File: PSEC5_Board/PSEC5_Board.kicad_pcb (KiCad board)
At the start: 6 copper layers, 76.2 x 76.2 mm, 187 parts, among them IC1 LTC6409IUDB#TRMPBF, IC2 LTC6409IUDB#TRMPBF, IC3 LTC6409IUDB#TRMPBF, IC4 LTC6409IUDB#TRMPBF, IC5 LTC6409IUDB#TRMPBF, IC6 LTC6409IUDB#TRMPBF, IC7 LTC6409IUDB#TRMPBF, IC8 LTC6409IUDB#TRMPBF, J1 QTH-040-01-X-D-DP-A, J11 Conn_Coaxial, J2 Conn_Coaxial, J3 Conn_Coaxial, J4 Conn_Coaxial, J5 Conn_Coaxial, J6 Conn_Coaxial, J7 Conn_Coaxial, J8 Conn_Coaxial, J9 QTH-040-01-X-D-DP-A, U1 MCP1700T-1802E_TT, U3 DAC8411IDCKT, U4 MC100LVEL40DWG, U6 OPA607QDBVRQ1, U7 AD4008BCPZ-RL7, Y1 ASE2-40.000MHZ-ET

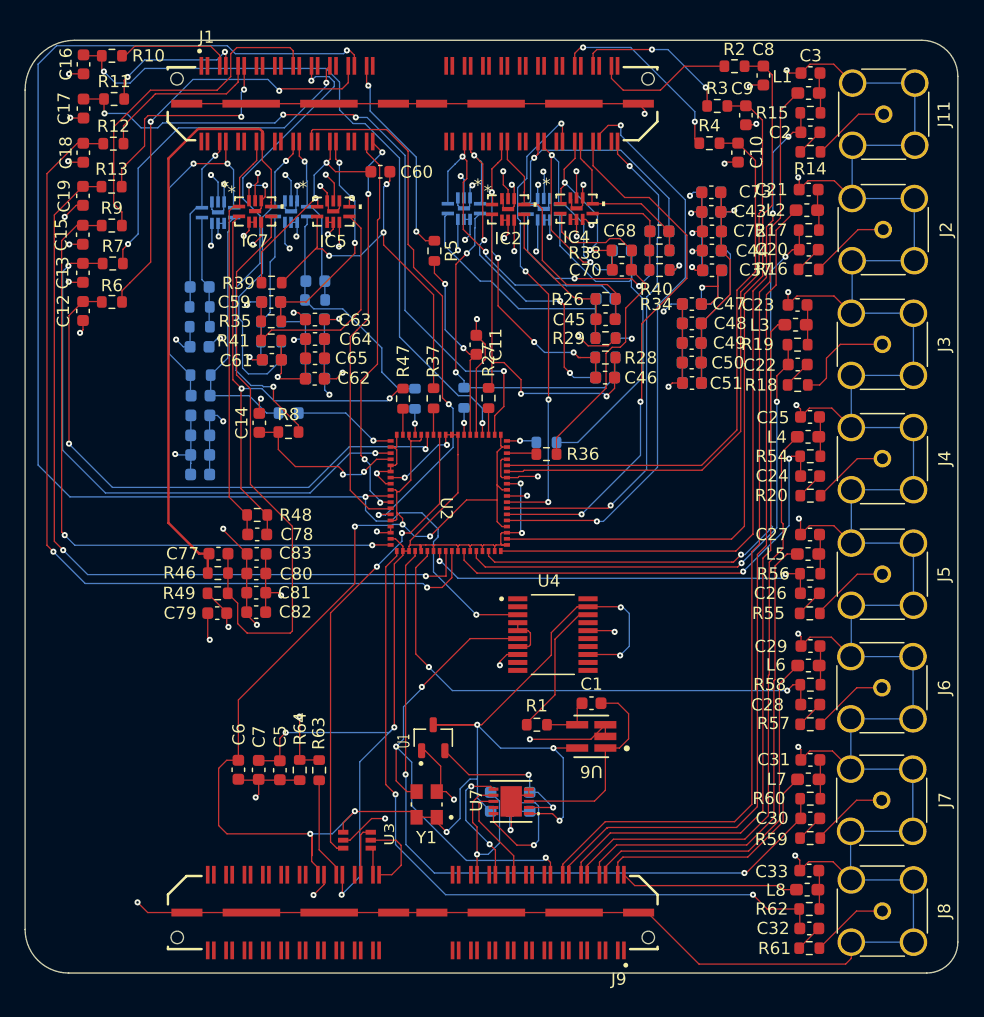
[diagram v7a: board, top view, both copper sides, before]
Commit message: DUT v4 Push
Addressed the issues discussed in last week's meeting, cleared ERC errors, still any warnings with Solder Mask.
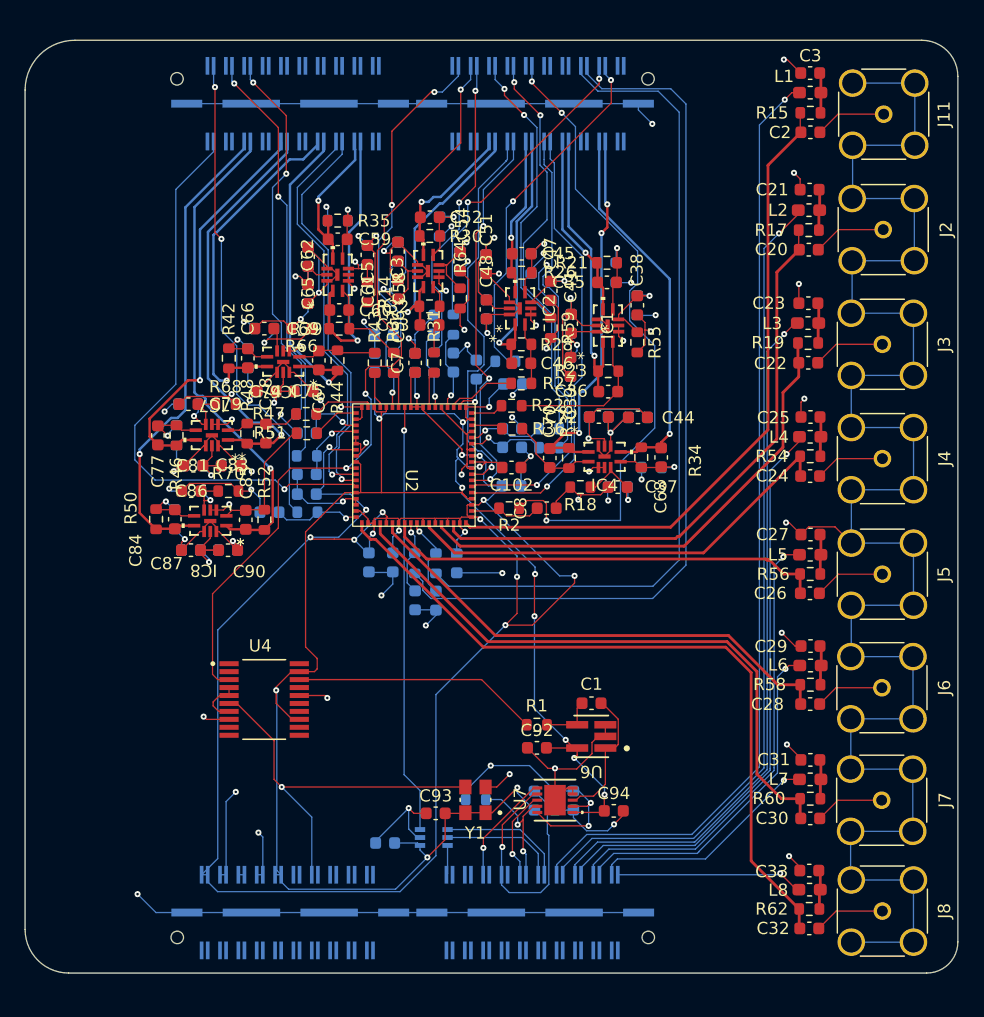
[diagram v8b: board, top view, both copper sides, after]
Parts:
- removed C6: 400n, Capacitor_SMD:C_0603_1608Metric
- removed U1: MCP1700T-1802E_TT, MCP1700T_1802E_TT:SOT95P237X112-3N
- added C100: 680n, Capacitor_SMD:C_0603_1608Metric, B.Cu at (145.0, 86.5)
- added C101: 100n, Capacitor_SMD:C_0603_1608Metric, B.Cu at (143.0, 86.5)
- added C102: 100n, Capacitor_SMD:C_0603_1608Metric, F.Cu at (154.7, 78.7)
- added C91: 0.1u, Capacitor_SMD:C_0603_1608Metric, B.Cu at (144.3, 109.4)
- added C92: 0.1u, Capacitor_SMD:C_0603_1608Metric, F.Cu at (156.8, 101.6)
- added C93: 0.1u, Capacitor_SMD:C_0603_1608Metric, F.Cu at (148.5, 107.0)
- added C94: 0.1u, Capacitor_SMD:C_0603_1608Metric, F.Cu at (163.0, 106.8)
- added C95: 330n, Capacitor_SMD:C_0603_1608Metric, B.Cu at (137.9, 80.9)
- added C96: 680n, Capacitor_SMD:C_0603_1608Metric, B.Cu at (154.8, 71.9)
- added C97: 680n, Capacitor_SMD:C_0603_1608Metric, B.Cu at (146.8, 70.2)
- added C98: 100n, Capacitor_SMD:C_0603_1608Metric, B.Cu at (154.7, 80.2)
- added C99: 330n, Capacitor_SMD:C_0603_1608Metric, B.Cu at (150.2, 86.5)
- added R65: 10k, Resistor_SMD:R_0603_1608Metric, B.Cu at (151.8, 105.8)
- added R66: 2k, Resistor_SMD:R_0603_1608Metric, F.Cu at (137.5, 67.4)
- added R67: 2k, Resistor_SMD:R_0603_1608Metric, B.Cu at (134.5, 67.4)
- added R68: 2k, Resistor_SMD:R_0603_1608Metric, F.Cu at (131.3, 73.5)
- added R69: 2k, Resistor_SMD:R_0603_1608Metric, B.Cu at (128.3, 73.5)
- added R70: 2k, Resistor_SMD:R_0603_1608Metric, F.Cu at (131.5, 80.7)
- added R71: 2k, Resistor_SMD:R_0603_1608Metric, B.Cu at (128.5, 80.7)
- C10, C11, C12, C13, C14, C15, C16, C17, C18, C19, C43, C49, C50, C63, C64, C73, C80, C82, C9, J1, J9, R10, R11, R12, R13, R29, R3, R4, R40, R41, R49, R5, R6, R63, R7, R8, R9, U3: moved to B.Cu
- C35, C36, C38, C39, C41, C52, C53, C54, C56, C58, C66, C67, C69, C74, C75, C84, C85, C86, C87, C90, IC1, IC3, IC6, IC8, R21, R22, R23, R30, R31, R32, R42, R43, R44, R50, R51, R52: moved to F.Cu
- C5: value 700n -> 330n; moved to B.Cu
- C7: value 100n -> 10p
- R14, R18, R55, R59: value 50 -> 2k
- R16, R57, R61: value 50 -> 2k; moved to B.Cu
- R20: value R_US -> 2k; moved to B.Cu
- moved R61 57.7 mm to (157.9, 64.3), turned to 90 degrees
- moved R59 46.8 mm to (157.9, 67.3), turned to -90 degrees
- moved C18 46.6 mm to (148.5, 89.6)
- moved R12 43.2 mm to (148.5, 86.5), turned to -90 degrees
- moved R63 43.1 mm to (150.5, 61.9)
- moved C19 42.8 mm to (146.8, 89.6)
- moved R64 40.7 mm to (150.5, 64.9)
- moved R2 40.5 mm to (154.5, 82.0), turned to 0 degrees
- moved C8 39.5 mm to (157.6, 82.0), turned to 0 degrees
- moved R13 39.5 mm to (146.8, 86.5), turned to -90 degrees
- moved C16 38.8 mm to (149.9, 70.2), turned to 90 degrees
- moved C17 38.5 mm to (151.8, 70.7), turned to 90 degrees
- moved R11 38.5 mm to (154.2, 70.0)
- moved R14 38.0 mm to (142.9, 64.4), turned to -90 degrees
- moved R57 37.0 mm to (164.9, 65.5), turned to 90 degrees
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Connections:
- C2 pad 2: Net-(C2-Pad2) -> Net-(J11-In)
- C20 pad 2: Net-(C20-Pad2) -> Net-(J2-In)
- C22 pad 2: Net-(C22-Pad2) -> Net-(J3-In)
- C24 pad 2: Net-(C24-Pad2) -> Net-(J4-In)
- C26 pad 2: Net-(C26-Pad2) -> Net-(J5-In)
- C28 pad 2: Net-(C28-Pad2) -> Net-(J6-In)
- C30 pad 2: Net-(C30-Pad2) -> Net-(J7-In)
- C32 pad 2: Net-(C32-Pad2) -> Net-(J8-In)
- C34 pad 1: Net-(U1-VOUT) -> VDD18
- C37 pad 1: V_OCM -> Net-(IC4-VOCM)
- C38 pad 1: V_OCM -> Net-(IC1-VOCM)
- C4 pad 2: Net-(U7-SDI) -> VDD18
- C47 pad 1: V_OCM -> Net-(IC2-VOCM)
- C5 pad 1: VDD -> GND
- C5 pad 2: GND -> VDD25
- C54 pad 1: V_OCM -> Net-(IC3-VOCM)
- C61 pad 1: V_OCM -> Net-(IC5-VOCM)
- C69 pad 1: V_OCM -> Net-(IC6-VOCM)
- C79 pad 1: V_OCM -> Net-(IC7-VOCM)
- C86 pad 1: V_OCM -> Net-(IC8-VOCM)
- IC1 pad 5: V_OCM -> Net-(IC1-VOCM)
- IC2 pad 5: V_OCM -> Net-(IC2-VOCM)
- IC3 pad 5: V_OCM -> Net-(IC3-VOCM)
- IC4 pad 5: V_OCM -> Net-(IC4-VOCM)
- IC5 pad 5: V_OCM -> Net-(IC5-VOCM)
- IC6 pad 5: V_OCM -> Net-(IC6-VOCM)
- IC7 pad 5: V_OCM -> Net-(IC7-VOCM)
- IC8 pad 5: V_OCM -> Net-(IC8-VOCM)
- J1 pad 05: READBIAS1 -> READBIAS2
- J1 pad 06: ADC8_Out- -> ADC1_Out+
- J1 pad 07: READBIAS2 -> READBIAS1
- J1 pad 08: ADC8_Out+ -> ADC1_Out-
- J1 pad 09: WBUFBIAS -> DISCBIAS
- J1 pad 11: DISCBIAS -> WBUFBIAS
- J1 pad 14: ADC7_Out+ -> ADC2_Out+
- J1 pad 16: ADC7_Out- -> ADC2_Out-
- J1 pad 18: unconnected-(J1-Pad18) -> SPIclk
- J1 pad 20: unconnected-(J1-Pad20) -> rst
- J1 pad 21: Disc_Thresh8 -> Disc_Thresh1
- J1 pad 22: ADC6_Out- -> ADC3_Out+
- J1 pad 24: ADC6_Out+ -> ADC3_Out-
- J1 pad 25: Disc_Thresh7 -> Disc_Thresh2
- J1 pad 26: TRIGGERIN -> POCI
- J1 pad 28: unconnected-(J1-Pad28) -> PICO
- J1 pad 29: Disc_Thresh6 -> Disc_Thresh3
- J1 pad 30: ADC5_Out+ -> ADC4_Out+
- J1 pad 32: ADC5_Out- -> ADC4_Out-
- J1 pad 33: Disc_Thresh5 -> Disc_Thresh4
- J1 pad 37: Disc_Thresh4 -> Disc_Thresh5
- J1 pad 38: ReadClk -> unconnected-(J1-Pad38)
- J1 pad 40: TRIGGEROUT -> unconnected-(J1-Pad40)
- J1 pad 46: ADC4_Out- -> ADC5_Out+
- J1 pad 48: ADC4_Out+ -> ADC5_Out-
- J1 pad 50: unconnected-(J1-Pad50) -> TRIGGEROUT
- J1 pad 52: unconnected-(J1-Pad52) -> ReadClk
- J1 pad 54: ADC3_Out+ -> ADC6_Out+
- J1 pad 56: ADC3_Out- -> ADC6_Out-
- J1 pad 62: ADC2_Out- -> ADC7_Out+
- J1 pad 64: ADC2_Out+ -> ADC7_Out-
- J1 pad 68: PICO -> unconnected-(J1-Pad68)
- J1 pad 69: Disc_Thresh3 -> Disc_Thresh6
- J1 pad 70: ADC1_Out+ -> ADC8_Out+
- J1 pad 72: ADC1_Out- -> ADC8_Out-
- J1 pad 73: Disc_Thresh2 -> Disc_Thresh7
- J1 pad 74: rst -> unconnected-(J1-Pad74)
- J1 pad 76: SPIclk -> unconnected-(J1-Pad76)
- J1 pad 77: Disc_Thresh1 -> Disc_Thresh8
- J1 pad 78: unconnected-(J1-Pad78) -> TRIGGERIN
- J1 pad 80: POCI -> unconnected-(J1-Pad80)
- J9 pad 02: V_ped8 -> VDD
- J9 pad 04: V_ped7 -> VDD
- J9 pad 06: V_ped6 -> VDD33
- J9 pad 08: V_ped5 -> VDD33
- J9 pad 10: V_ped4 -> VDD50
- J9 pad 12: V_ped3 -> VDD50
- J9 pad 14: V_ped2 -> VDD18
- J9 pad 16: V_ped1 -> VDD18
- J9 pad 18: CLK_OUT -> VDD25
- J9 pad 20: unconnected-(J9-Pad20) -> VDD25
- J9 pad 26: ADC_SCK -> CLK_OUT
- J9 pad 30: ADC_CNV -> unconnected-(J9-Pad30)
- J9 pad 34: ADC_SDO -> unconnected-(J9-Pad34)
- J9 pad 42: DAC_SCLK -> DAC_V_IN
- J9 pad 44: SYNC_N -> unconnected-(J9-Pad44)
- J9 pad 46: DAC_V_IN -> unconnected-(J9-Pad46)
- J9 pad 50: VDD -> ADC_CNV
- J9 pad 52: VDD18 -> unconnected-(J9-Pad52)
- J9 pad 54: VDD33 -> ADC_SDO
- J9 pad 56: VDD25 -> unconnected-(J9-Pad56)
- J9 pad 58: VDD50 -> ADC_SCK
- J9 pad 60: unconnected-(J9-Pad60) -> ADC_SDI
- J9 pad 62: unconnected-(J9-Pad62) -> DAC_SCLK
- J9 pad 64: unconnected-(J9-Pad64) -> SYNC_N
- J9 pad 66: unconnected-(J9-Pad66) -> V_ped1
- J9 pad 68: unconnected-(J9-Pad68) -> V_ped2
- J9 pad 70: unconnected-(J9-Pad70) -> V_ped3
- J9 pad 72: unconnected-(J9-Pad72) -> V_ped4
- J9 pad 74: unconnected-(J9-Pad74) -> V_ped5
- J9 pad 76: unconnected-(J9-Pad76) -> V_ped6
- J9 pad 78: unconnected-(J9-Pad78) -> V_ped7
- J9 pad 80: unconnected-(J9-Pad80) -> V_ped8
- R14 pad 1: Net-(C2-Pad2) -> Net-(IC5-VOCM)
- R14 pad 2: Net-(J11-In) -> GND
- R16 pad 1: Net-(C20-Pad2) -> VDD18
- R16 pad 2: Net-(J2-In) -> Net-(IC5-VOCM)
- R18 pad 1: Net-(C22-Pad2) -> Net-(IC4-VOCM)
- R18 pad 2: Net-(J3-In) -> GND
- R20 pad 1: Net-(C24-Pad2) -> VDD18
- R20 pad 2: Net-(J4-In) -> Net-(IC4-VOCM)
- R55 pad 1: Net-(C26-Pad2) -> Net-(IC1-VOCM)
- R55 pad 2: Net-(J5-In) -> GND
- R57 pad 1: Net-(C28-Pad2) -> VDD18
- R57 pad 2: Net-(J6-In) -> Net-(IC1-VOCM)
- R59 pad 1: Net-(C30-Pad2) -> Net-(IC2-VOCM)
- R59 pad 2: Net-(J7-In) -> GND
- R61 pad 1: Net-(C32-Pad2) -> VDD18
- R61 pad 2: Net-(J8-In) -> Net-(IC2-VOCM)
- R63 pad 2: V_OCM -> Net-(IC3-VOCM)
- R64 pad 1: V_OCM -> Net-(IC3-VOCM)
- U7 pad 10: Net-(U7-SDI) -> VDD18
- U7 pad 2: Net-(U1-VOUT) -> VDD18
- U7 pad 9: Net-(U7-SDI) -> ADC_SDI
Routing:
- net VDD: track 85.7 -> 173.4 mm, vias 7 -> 16
- net /Biases,Thresh/wbufbias_postrc: track 73.0 -> 6.71 mm, vias 2 -> 1
- net /Biases,Thresh/discbias_postrc: track 66.7 -> 6.19 mm, vias 2 -> 1
- net /Biases,Thresh/discthresh1_postrc: track 60.2 -> 5.94 mm
- net WBUFBIAS: track 13.6 -> 67.8 mm
- net DISCBIAS: track 19.1 -> 72.0 mm, vias 2 -> 0
- net /Biases,Thresh/readbias2_postrc: track 58.0 -> 5.68 mm, vias 4 -> 1
- net /Biases,Thresh/readbias1_postrc: track 58.2 -> 6.61 mm, vias 2 -> 1
- net /Biases,Thresh/discthresh8_postrc: track 54.9 -> 7.04 mm, vias 2 -> 1
- net PSEC5_CLK_OUT: track 110.7 -> 66.7 mm
- net /Biases,Thresh/discthresh2_postrc: track 50.0 -> 6.54 mm, vias 0 -> 1
- net /Biases,Thresh/discthresh6_postrc: track 47.7 -> 5.18 mm, vias 2 -> 1
- net Net-(IC7--IN): track 47.9 -> 5.57 mm, vias 0 -> 1
- net Disc_Thresh1: track 11.5 -> 53.0 mm, vias 0 -> 3
- net /Biases,Thresh/discthresh5_postrc: track 47.0 -> 6.45 mm, vias 2 -> 1
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- added copper zone on In3.Cu, net VDD18
- removed copper zone on In3.Cu, net V_OCM
